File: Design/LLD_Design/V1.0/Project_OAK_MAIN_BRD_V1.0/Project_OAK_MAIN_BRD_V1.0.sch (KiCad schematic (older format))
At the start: 96 parts, among them U1 ATmega328PB-MU, U2 RV-8263-C7-32.768KHZ-20PPM-TA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

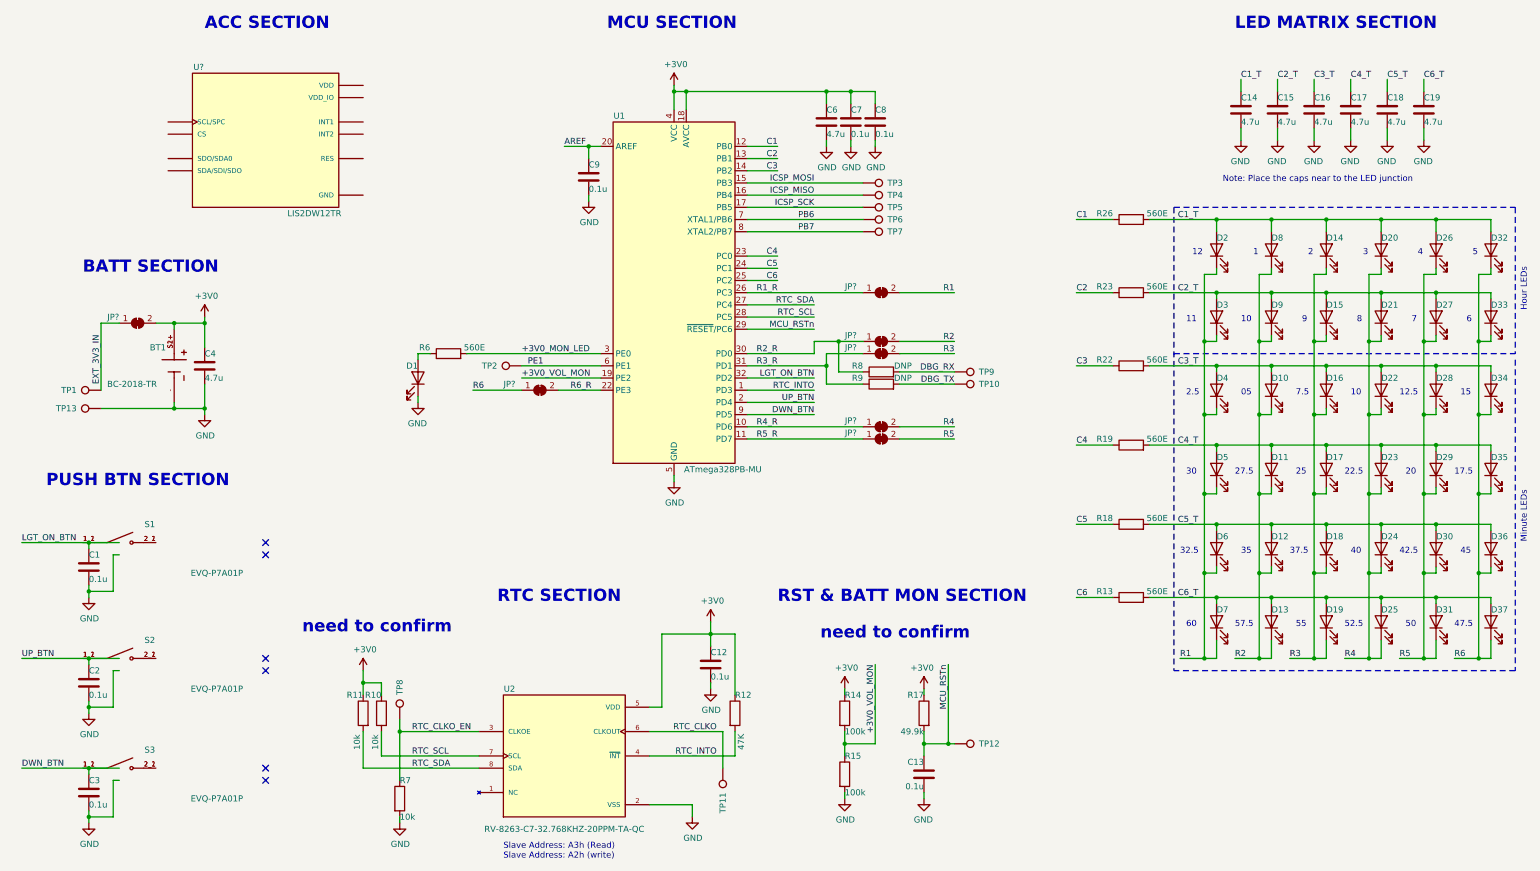
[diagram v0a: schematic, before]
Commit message: Added V1.0 pinmap data and update schematics
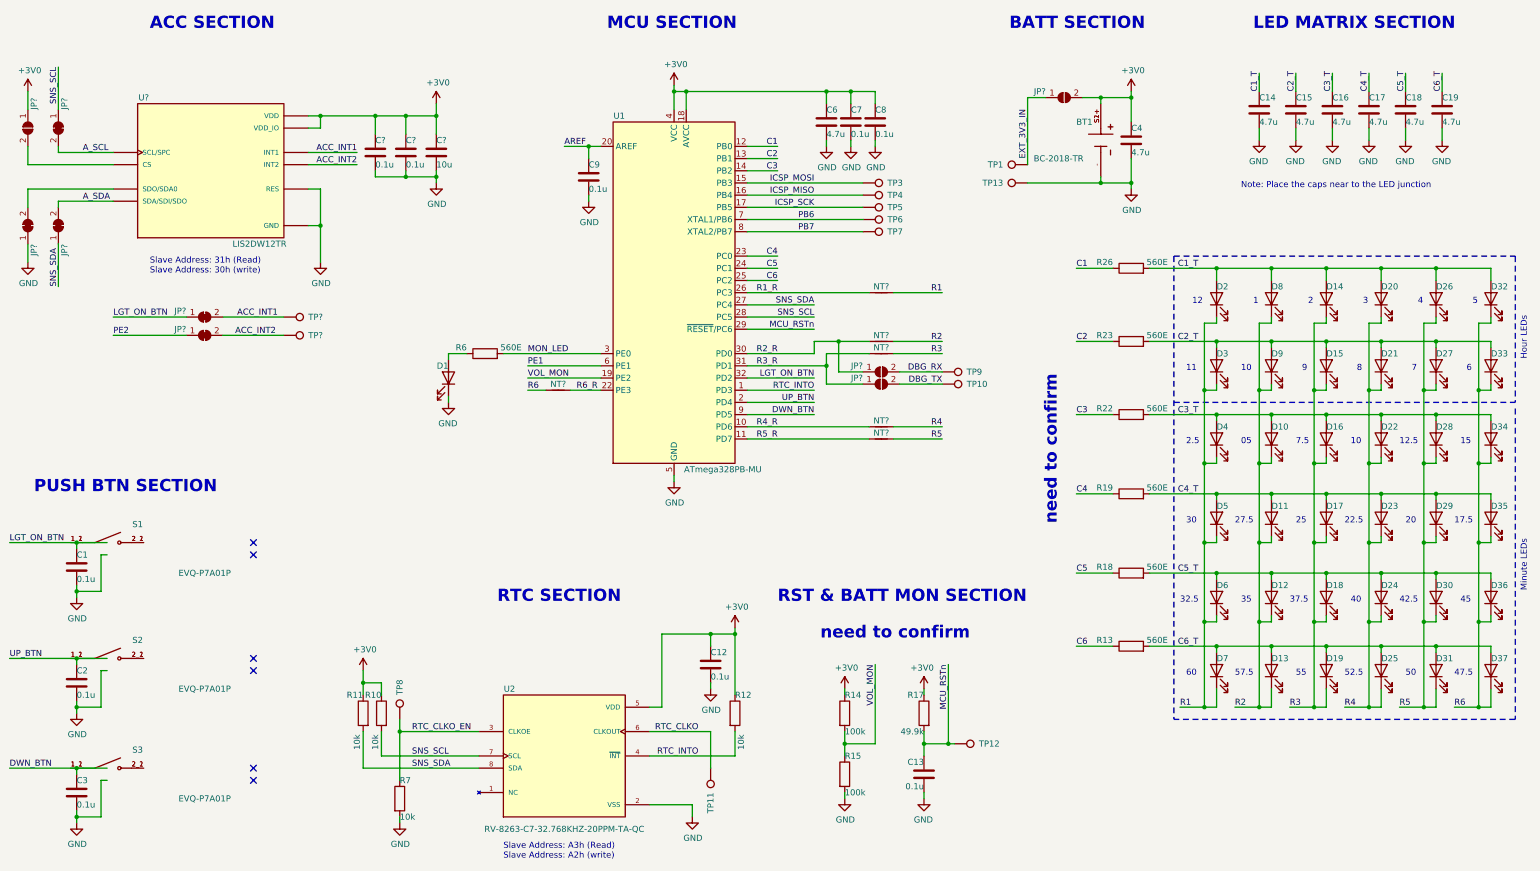
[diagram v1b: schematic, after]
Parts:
- removed JP? (x7): SolderJumper_2_Bridged, symbol Jumper:SolderJumper_2_Bridged
- removed R8, R9: DNP, Resistor_SMD:R_0402_1005Metric, symbol Device:R
- removed TP2: TestPoint, TestPoint:TestPoint_Pad_D1.0mm, symbol Connector:TestPoint
- added C? (x2): 0.1u, Capacitor_SMD:C_0402_1005Metric, symbol Device:C
- added C?: 10u, Capacitor_SMD:C_0402_1005Metric, symbol Device:C
- added JP? (x5): SolderJumper_2_Bridged, symbol Jumper:SolderJumper_2_Bridged
- added JP? (x4): SolderJumper_2_Open, symbol Jumper:SolderJumper_2_Open
- added NT? (x6): Net-Tie_2, symbol Device:Net-Tie_2
- added TP? (x2): TestPoint, TestPoint:TestPoint_Pad_D1.0mm, symbol Connector:TestPoint
- R12: value 47K -> 10k
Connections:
- net labels added: ACC_INT1, ACC_INT2, A_SCL, A_SDA, MON_LED, PE2, SNS_SCL, SNS_SDA, VOL_MON
- net labels removed: +3V0_MON_LED, +3V0_VOL_MON, RTC_SCL, RTC_SDA
- wire segments 338 -> 376
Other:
- note added: "Slave Address: 31h (Read)\nSlave Address: 30h (write)"
- moved on the sheet: BT1, C1, C14, C15, C16, C17, C18, C19, C2, C3, C4, D1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

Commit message: imported net list into layout
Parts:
- removed TP? (x2): TestPoint, TestPoint:TestPoint_Pad_D1.0mm, symbol Connector:TestPoint
- BT1: footprint BAT_BC-2018-TR -> Battery:BAT_BC-2018-TR
- JP1, JP7, JP8, JP9: renamed from JP?; footprint (none) -> Jumper:SolderJumper-2_P1.3mm_Open_RoundedPad1.0x1.5mm
- JP2, JP3, JP4, JP5, JP6: renamed from JP?; footprint (none) -> Jumper:SolderJumper-2_P1.3mm_Bridged_RoundedPad1.0x1.5mm
- NT1, NT2, NT3, NT4, NT5, NT6: renamed from NT?; footprint (none) -> NetTie:NetTie-2_SMD_Pad0.5mm
- U3: renamed from U?; footprint LGA12R50P4X4_200X200X70 -> Sensor:LIS2DW12TR
- gave numbers to parts that had none: 3
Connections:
- net labels removed: PE2
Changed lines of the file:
@@
 Text Label 6550 6800 2    50   ~ 0
 RTC_INTO
-Text Notes 4900 5550 0    100  ~ 20
-RTC SECTION
 Text Notes 1100 4650 0    100  ~ 20
 PUSH BTN SECTION
@@
 F 0 "BT1" V 9700 1550 50  0000 L CNN
 F 1 "BC-2018-TR" V 10000 1200 50  0000 L CNN
-F 2 "BAT_BC-2018-TR" H 9850 1750 50  0001 L BNN
+F 2 "Battery:BAT_BC-2018-TR" H 9850 1750 50  0001 L BNN
 F 3 "" H 9850 1750 50  0001 L BNN
 F 4 "MPD (Memory Protection Devices)" H 9850 1750 50  0001 L BNN "MF"
@@
 Connection ~ 10100 2100
 $Comp
-L LIS2DW12TR:LIS2DW12TR U?
+L LIS2DW12TR:LIS2DW12TR U3
 U 1 1 68D2D363
 P 2550 1950
-F 0 "U?" H 2000 2500 50  0000 C CNN
+F 0 "U3" H 2000 2500 50  0000 C CNN
 F 1 "LIS2DW12TR" H 2950 1300 50  0000 C CNN
-F 2 "LGA12R50P4X4_200X200X70" H 2550 1950 50  0001 L BNN
+F 2 "Sensor:LIS2DW12TR" H 2550 1950 50  0001 L BNN
 F 3 "" H 2550 1950 50  0001 L BNN
 F 4 "STMicroelectronics" H 2550 1950 50  0001 L BNN "MF"
@@
 $EndComp
 $Comp
-L power:GND #PWR?
+L power:GND #PWR05
 U 1 1 68D3E761
 P 3450 2750
-F 0 "#PWR?" H 3450 2500 50  0001 C CNN
+F 0 "#PWR05" H 3450 2500 50  0001 C CNN
 F 1 "GND" H 3455 2577 50  0000 C CNN
 F 2 "" H 3450 2750 50  0001 C CNN
@@
 ACC_INT2
 $Comp
-L power:+3V0 #PWR?
+L power:+3V0 #PWR09
 U 1 1 68E86F57
 P 4400 1450
-F 0 "#PWR?" H 4400 1300 50  0001 C CNN
+F 0 "#PWR09" H 4400 1300 50  0001 C CNN
 F 1 "+3V0" H 4415 1623 50  0000 C CNN
 F 2 "" H 4400 1450 50  0001 C CNN
@@
 $EndComp
 $Comp
-L Device:C C?
+L Device:C C5
 U 1 1 68EAAFD1
 P 3900 1850
-F 0 "C?" H 3900 1950 50  0000 L CNN
+F 0 "C5" H 3900 1950 50  0000 L CNN
 F 1 "0.1u" H 3900 1750 50  0000 L CNN
 F 2 "Capacitor_SMD:C_0402_1005Metric" H 3938 1700 50  0001 C CNN
@@
 	3900 2000 3900 2050
 $Comp
-L Device:C C?
+L Device:C C10
 U 1 1 68ECD6BD
 P 4150 1850
-F 0 "C?" H 4150 1950 50  0000 L CNN
+F 0 "C10" H 4150 1950 50  0000 L CNN
 F 1 "0.1u" H 4150 1750 50  0000 L CNN
 F 2 "Capacitor_SMD:C_0402_1005Metric" H 4188 1700 50  0001 C CNN
@@
 	4150 2000 4150 2050
 $Comp
-L Device:C C?
+L Device:C C11
 U 1 1 68EEF466
 P 4400 1850
-F 0 "C?" H 4400 1950 50  0000 L CNN
+F 0 "C11" H 4400 1950 50  0000 L CNN
 F 1 "10u" H 4400 1750 50  0000 L CNN
 F 2 "Capacitor_SMD:C_0402_1005Metric" H 4438 1700 50  0001 C CNN
@@
 $EndComp
 $Comp
-L power:GND #PWR?
+L power:GND #PWR011
 U 1 1 68EEF470
 P 4400 2100
-F 0 "#PWR?" H 4400 1850 50  0001 C CNN
+F 0 "#PWR011" H 4400 1850 50  0001 C CNN
 F 1 "GND" H 4405 1927 50  0000 C CNN
 F 2 "" H 4400 2100 50  0001 C CNN
@@
 	4400 1550 4400 1700
 Connection ~ 4150 1550
-$Comp
-L Connector:TestPoint TP?
-U 1 1 68FC99E1
-P 3150 3200
-F 0 "TP?" V 3150 3400 50  0000 L CNN
-F 1 "TestPoint" H 3208 3227 50  0001 L CNN
-F 2 "TestPoint:TestPoint_Pad_D1.0mm" H 3350 3200 50  0001 C CNN
-F 3 "~" H 3350 3200 50  0001 C CNN
-	1    3150 3200
-	0    1    1    0
-$EndComp
 Wire Wire Line
 	4150 2050 4400 2050
@@
 	1300 2950 1300 2600
 $Comp
-L Jumper:SolderJumper_2_Bridged JP?
+L Jumper:SolderJumper_2_Bridged JP4
 U 1 1 693258B0
 P 1300 2450
-F 0 "JP?" H 1100 2500 50  0000 C CNN
+F 0 "JP4" H 1100 2500 50  0000 C CNN
 F 1 "SolderJumper_2_Bridged" H 1300 2564 50  0001 C CNN
-F 2 "" H 1300 2450 50  0001 C CNN
+F 2 "Jumper:SolderJumper-2_P1.3mm_Bridged_RoundedPad1.0x1.5mm" H 1300 2450 50  0001 C CNN
 F 3 "~" H 1300 2450 50  0001 C CNN
 	1    1300 2450
@@
 $EndComp
 $Comp
-L Jumper:SolderJumper_2_Bridged JP?
+L Jumper:SolderJumper_2_Bridged JP3
 U 1 1 6939B47C
 P 1300 1650
-F 0 "JP?" H 1100 1700 50  0000 C CNN
+F 0 "JP3" H 1100 1700 50  0000 C CNN
 F 1 "SolderJumper_2_Bridged" H 1300 1764 50  0001 C CNN
-F 2 "" H 1300 1650 50  0001 C CNN
+F 2 "Jumper:SolderJumper-2_P1.3mm_Bridged_RoundedPad1.0x1.5mm" H 1300 1650 50  0001 C CNN
 F 3 "~" H 1300 1650 50  0001 C CNN
 	1    1300 1650
@@
 A_SCL
 $Comp
-L power:GND #PWR?
+L power:GND #PWR03
 U 1 1 69461174
 P 1050 2750
-F 0 "#PWR?" H 1050 2500 50  0001 C CNN
+F 0 "#PWR03" H 1050 2500 50  0001 C CNN
 F 1 "GND" H 1055 2577 50  0000 C CNN
 F 2 "" H 1050 2750 50  0001 C CNN
@@
 	1050 2150 1750 2150
 $Comp
-L power:+3V0 #PWR?
+L power:+3V0 #PWR01
 U 1 1 695C981D
 P 1050 1350
-F 0 "#PWR?" H 1050 1200 50  0001 C CNN
+F 0 "#PWR01" H 1050 1200 50  0001 C CNN
 F 1 "+3V0" H 1065 1523 50  0000 C CNN
 F 2 "" H 1050 1350 50  0001 C CNN
@@
 RST & BATT MON SECTION
 $Comp
-L Connector:TestPoint TP?
-U 1 1 6901336B
-P 3150 3350
-F 0 "TP?" V 3150 3550 50  0000 L CNN
-F 1 "TestPoint" H 3208 3377 50  0001 L CNN
-F 2 "TestPoint:TestPoint_Pad_D1.0mm" H 3350 3350 50  0001 C CNN
-F 3 "~" H 3350 3350 50  0001 C CNN
-	1    3150 3350
-	0    1    1    0
-$EndComp
-$Comp
-L Jumper:SolderJumper_2_Bridged JP?
+L Jumper:SolderJumper_2_Bridged JP5
 U 1 1 6A1A2DD4
 P 2500 3200
-F 0 "JP?" H 2300 3250 50  0000 C CNN
+F 0 "JP5" H 2300 3250 50  0000 C CNN
 F 1 "SolderJumper_2_Bridged" H 2500 3314 50  0001 C CNN
-F 2 "" H 2500 3200 50  0001 C CNN
+F 2 "Jumper:SolderJumper-2_P1.3mm_Bridged_RoundedPad1.0x1.5mm" H 2500 3200 50  0001 C CNN
 F 3 "~" H 2500 3200 50  0001 C CNN
 	1    2500 3200
@@
 LGT_ON_BTN
 $Comp
-L Jumper:SolderJumper_2_Bridged JP?
+L Jumper:SolderJumper_2_Bridged JP6
 U 1 1 6A3743CA
 P 2500 3350
-F 0 "JP?" H 2300 3400 50  0000 C CNN
+F 0 "JP6" H 2300 3400 50  0000 C CNN
 F 1 "SolderJumper_2_Bridged" H 2500 3464 50  0001 C CNN
-F 2 "" H 2500 3350 50  0001 C CNN
+F 2 "Jumper:SolderJumper-2_P1.3mm_Bridged_RoundedPad1.0x1.5mm" H 2500 3350 50  0001 C CNN
 F 3 "~" H 2500 3350 50  0001 C CNN
 	1    2500 3350
@@
 	3350 1950 3750 1950
 Text Label 1750 3350 0    50   ~ 0
-PE2
+PE1
 Wire Wire Line
 	11150 1200 11150 1350
@@
 Slave Address: 31h (Read)\nSlave Address: 30h (write)
 $Comp
-L Jumper:SolderJumper_2_Bridged JP?
+L Jumper:SolderJumper_2_Bridged JP2
 U 1 1 6A881C6E
 P 1050 2450
-F 0 "JP?" H 850 2500 50  0000 C CNN
+F 0 "JP2" H 850 2500 50  0000 C CNN
 F 1 "SolderJumper_2_Bridged" H 1050 2564 50  0001 C CNN
-F 2 "" H 1050 2450 50  0001 C CNN
+F 2 "Jumper:SolderJumper-2_P1.3mm_Bridged_RoundedPad1.0x1.5mm" H 1050 2450 50  0001 C CNN
 F 3 "~" H 1050 2450 50  0001 C CNN
 	1    1050 2450
@@
 $EndComp
 $Comp
-L Jumper:SolderJumper_2_Open JP?
+L Jumper:SolderJumper_2_Open JP1
 U 1 1 6A8D51C0
 P 1050 1650
-F 0 "JP?" H 850 1700 50  0000 C CNN
+F 0 "JP1" H 850 1700 50  0000 C CNN
 F 1 "SolderJumper_2_Open" H 1050 1764 50  0001 C CNN
-F 2 "" H 1050 1650 50  0001 C CNN
+F 2 "Jumper:SolderJumper-2_P1.3mm_Open_RoundedPad1.0x1.5mm" H 1050 1650 50  0001 C CNN
 F 3 "~" H 1050 1650 50  0001 C CNN
 	1    1050 1650
@@
 $EndComp
 $Comp
-L Jumper:SolderJumper_2_Open JP?
+L Jumper:SolderJumper_2_Open JP7
 U 1 1 6A97A748
 P 8050 3650
-F 0 "JP?" H 7850 3700 50  0000 C CNN
+F 0 "JP7" H 7850 3700 50  0000 C CNN
 F 1 "SolderJumper_2_Open" H 8050 3764 50  0001 C CNN
-F 2 "" H 8050 3650 50  0001 C CNN
+F 2 "Jumper:SolderJumper-2_P1.3mm_Open_RoundedPad1.0x1.5mm" H 8050 3650 50  0001 C CNN
 F 3 "~" H 8050 3650 50  0001 C CNN
 	1    8050 3650
@@
 $EndComp
 $Comp
-L Jumper:SolderJumper_2_Open JP?
+L Jumper:SolderJumper_2_Open JP8
 U 1 1 6A9CEA05
 P 8050 3750
-F 0 "JP?" H 7850 3800 50  0000 C CNN
+F 0 "JP8" H 7850 3800 50  0000 C CNN
 F 1 "SolderJumper_2_Open" H 8050 3864 50  0001 C CNN
-F 2 "" H 8050 3750 50  0001 C CNN
+F 2 "Jumper:SolderJumper-2_P1.3mm_Open_RoundedPad1.0x1.5mm" H 8050 3750 50  0001 C CNN
 F 3 "~" H 8050 3750 50  0001 C CNN
 	1    8050 3750
@@
 $EndComp
 $Comp
-L Device:Net-Tie_2 NT?
+L Device:Net-Tie_2 NT2
 U 1 1 6A9F87DC
 P 8050 3000
-F 0 "NT?" H 8050 3050 50  0000 C CNN
+F 0 "NT2" H 8050 3050 50  0000 C CNN
 F 1 "Net-Tie_2" H 8050 3090 50  0001 C CNN
-F 2 "" H 8050 3000 50  0001 C CNN
+F 2 "NetTie:NetTie-2_SMD_Pad0.5mm" H 8050 3000 50  0001 C CNN
 F 3 "~" H 8050 3000 50  0001 C CNN
 	1    8050 3000
@@
 	6950 3000 7950 3000
 $Comp
-L Device:Net-Tie_2 NT?
+L Device:Net-Tie_2 NT3
 U 1 1 6AAA1105
 P 8050 3400
-F 0 "NT?" H 8050 3450 50  0000 C CNN
+F 0 "NT3" H 8050 3450 50  0000 C CNN
 F 1 "Net-Tie_2" H 8050 3490 50  0001 C CNN
-F 2 "" H 8050 3400 50  0001 C CNN
+F 2 "NetTie:NetTie-2_SMD_Pad0.5mm" H 8050 3400 50  0001 C CNN
 F 3 "~" H 8050 3400 50  0001 C CNN
 	1    8050 3400
@@
 $EndComp
 $Comp
-L Device:Net-Tie_2 NT?
+L Device:Net-Tie_2 NT4
 U 1 1 6AAC9C1E
 P 8050 3500
-F 0 "NT?" H 8050 3550 50  0000 C CNN
+F 0 "NT4" H 8050 3550 50  0000 C CNN
 F 1 "Net-Tie_2" H 8050 3590 50  0001 C CNN
-F 2 "" H 8050 3500 50  0001 C CNN
+F 2 "NetTie:NetTie-2_SMD_Pad0.5mm" H 8050 3500 50  0001 C CNN
 F 3 "~" H 8050 3500 50  0001 C CNN
 	1    8050 3500
@@
 $EndComp
 $Comp
-L Device:Net-Tie_2 NT?
+L Device:Net-Tie_2 NT5
 U 1 1 6AB4359A
 P 8050 4100
-F 0 "NT?" H 8050 4150 50  0000 C CNN
+F 0 "NT5" H 8050 4150 50  0000 C CNN
 F 1 "Net-Tie_2" H 8050 4190 50  0001 C CNN
-F 2 "" H 8050 4100 50  0001 C CNN
+F 2 "NetTie:NetTie-2_SMD_Pad0.5mm" H 8050 4100 50  0001 C CNN
 F 3 "~" H 8050 4100 50  0001 C CNN
 	1    8050 4100
@@
 $EndComp
 $Comp
-L Device:Net-Tie_2 NT?
+L Device:Net-Tie_2 NT6
 U 1 1 6AB435A4
 P 8050 4200
-F 0 "NT?" H 8050 4250 50  0000 C CNN
+F 0 "NT6" H 8050 4250 50  0000 C CNN
 F 1 "Net-Tie_2" H 8050 4290 50  0001 C CNN
-F 2 "" H 8050 4200 50  0001 C CNN
+F 2 "NetTie:NetTie-2_SMD_Pad0.5mm" H 8050 4200 50  0001 C CNN
 F 3 "~" H 8050 4200 50  0001 C CNN
 	1    8050 4200
@@
 $EndComp
 $Comp
-L Device:Net-Tie_2 NT?
+L Device:Net-Tie_2 NT1
 U 1 1 6AC10768
 P 5400 3800
-F 0 "NT?" H 5400 3850 50  0000 C CNN
+F 0 "NT1" H 5400 3850 50  0000 C CNN
 F 1 "Net-Tie_2" H 5400 3890 50  0001 C CNN
-F 2 "" H 5400 3800 50  0001 C CNN
+F 2 "NetTie:NetTie-2_SMD_Pad0.5mm" H 5400 3800 50  0001 C CNN
 F 3 "~" H 5400 3800 50  0001 C CNN
 	1    5400 3800
@@
 $EndComp
 $Comp
-L Jumper:SolderJumper_2_Open JP?
+L Jumper:SolderJumper_2_Open JP9
 U 1 1 6ACB5424
 P 9550 1400
-F 0 "JP?" H 9350 1450 50  0000 C CNN
+F 0 "JP9" H 9350 1450 50  0000 C CNN
 F 1 "SolderJumper_2_Open" H 9550 1514 50  0001 C CNN
-F 2 "" H 9550 1400 50  0001 C CNN
+F 2 "Jumper:SolderJumper-2_P1.3mm_Open_RoundedPad1.0x1.5mm" H 9550 1400 50  0001 C CNN
 F 3 "~" H 9550 1400 50  0001 C CNN
 	1    9550 1400
@@
 Text Notes 9500 4900 1    100  ~ 20
 need to confirm
+Text Notes 4900 5550 0    100  ~ 20
+RTC SECTION
 $EndSCHEMATC
